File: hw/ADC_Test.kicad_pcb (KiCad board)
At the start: 2 copper layers, 50 x 32 mm, 63 parts, among them J1 SMA in (perfboard), J2 9V IN, J3 PMOD (ZedBoard), U1 OPA2365, U2 OPA2365, U3 THS4531, U4 ADS7057, U5 AMS1117-3.3, U6 LM393, U7 AMS1117-5.0

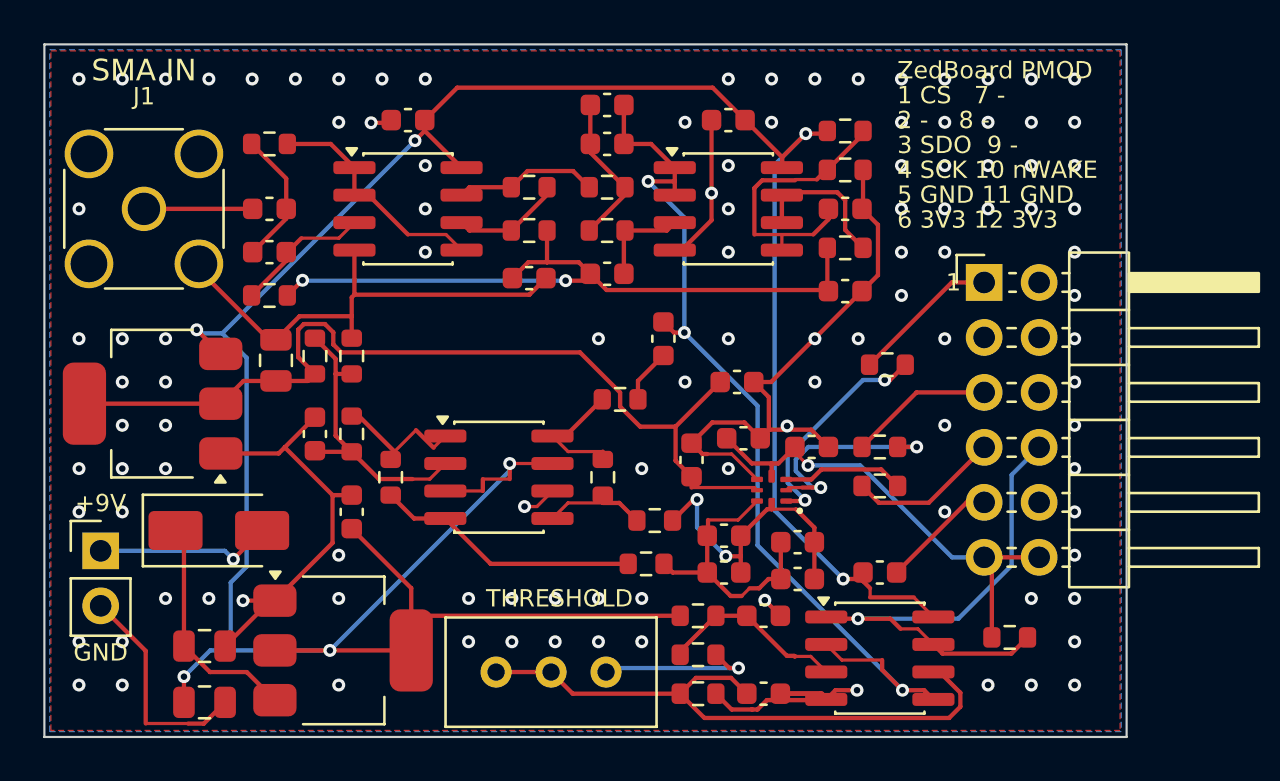
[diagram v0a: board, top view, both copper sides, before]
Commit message: Add MON output, nWAKE DNP cap, ceramic-stable AVDD LDO, M3 holes
- J4 SMA MON: LPF_OUT through 51R (Basic C23197)
- C31 0603 DNP on nWAKE near J3
- AVDD: XC6206P332 (Basic, ceramic-stable) replaces AMS1117-3.3
- 5 V AMS1117: 22 uF tantalum output per datasheet
- H1/H2 M3 holes, CH silkscreen field, PMOD legend on the back
- README: uses, regulator decision, MON/DNP

Co-Authored-By: Claude Opus 5.5 <noreply@anthropic.com>
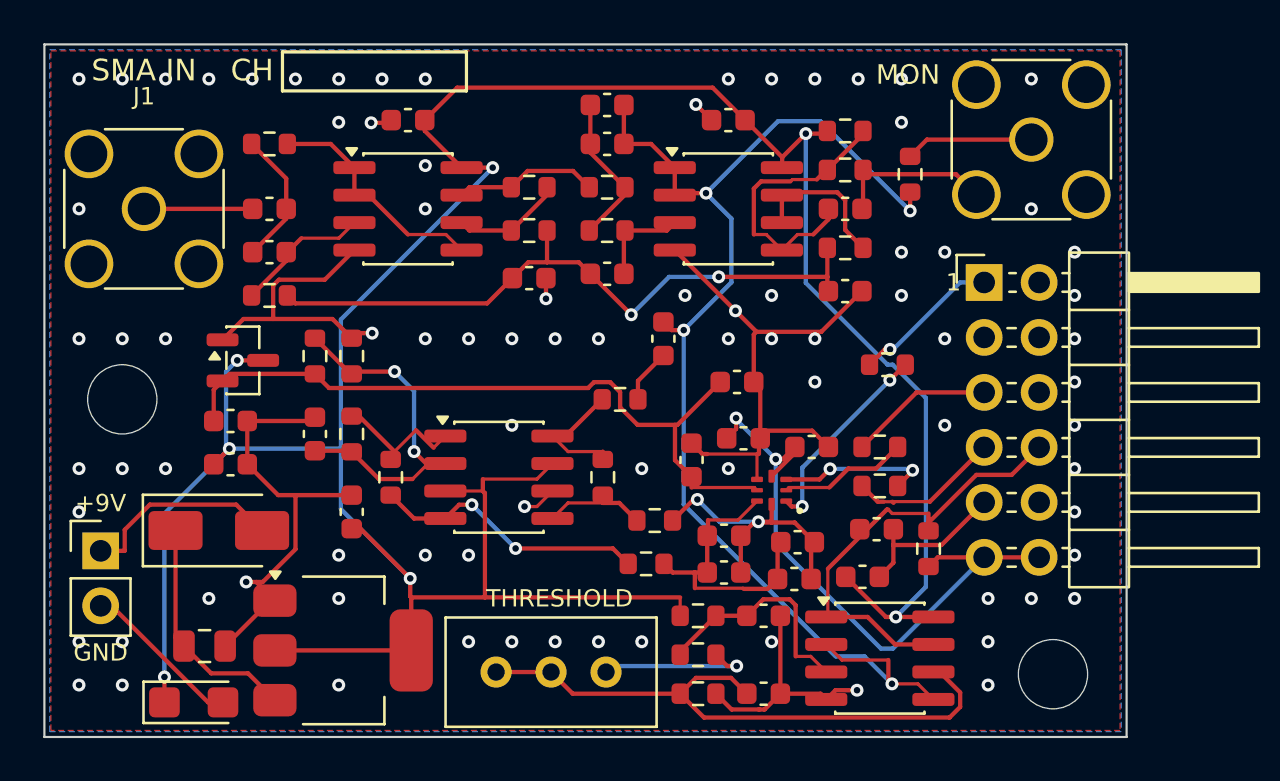
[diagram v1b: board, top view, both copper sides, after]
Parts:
- removed C24: 22uF 25V, Capacitor_SMD:C_0805_2012Metric
- added C29: 22uF 10V tantalum, Capacitor_Tantalum_SMD:CP_EIA-3216-18_Kemet-A, F.Cu at (106.9, 130.4)
- added C30: 1uF, Capacitor_SMD:C_0603_1608Metric, F.Cu at (108.6, 119.4)
- added C31: DNP, Capacitor_SMD:C_0603_1608Metric, F.Cu at (138.4, 122.4)
- added H1: M3, MountingHole:MountingHole_3.2mm_M3, F.Cu at (103.6, 116.4)
- added H2: M3, MountingHole:MountingHole_3.2mm_M3, F.Cu at (146.6, 129.1)
- added J4: SMA MON (hand-solder), Connector_Coaxial:SMA_Amphenol_132134_Vertical, F.Cu at (145.6, 104.4)
- added R25: 51R, Resistor_SMD:R_0603_1608Metric, F.Cu at (140.0, 106.0)
- C21: value 22uF 25V -> 1uF; footprint Capacitor_SMD:C_0805_2012Metric -> Capacitor_SMD:C_0603_1608Metric
- U5: value AMS1117-3.3 -> XC6206P332MR-G; footprint Package_TO_SOT_SMD:SOT-223-3_TabPin2 -> Package_TO_SOT_SMD:SOT-23
- moved R24 5.56 mm to (140.8, 123.3), turned to 90 degrees
- moved U5 4.62 mm to (109.2, 114.6), turned to 0 degrees
- moved C21 3.50 mm to (108.6, 117.4), turned to 0 degrees
- moved C28 0.82 mm to (137.8, 124.6)
- moved C17 0.15 mm to (134.7, 124.7)
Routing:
- net LPF_OUT: track 42.9 -> 57.3 mm, vias 3 -> 4
- net GND: track 107.0 -> 97.0 mm, vias 109 -> 84
- net AVDD: track 42.9 -> 33.9 mm
- net +3V3: track 21.6 -> 29.3 mm, vias 1 -> 2
- net MON: track 0.00 -> 5.92 mm
- net +5V: track 136.2 -> 141.3 mm
- net SDO_A: track 10.4 -> 5.98 mm, vias 2 -> 0
- net WAKE_N: track 24.4 -> 21.5 mm, vias 1 -> 0
- net VOCM: track 13.6 -> 16.2 mm, vias 0 -> 2
- net VMID5: track 33.3 -> 31.1 mm
- net VTH_H: track 8.66 -> 10.7 mm
- net SCLK_A: track 5.66 -> 7.07 mm, vias 0 -> 2
- net +9V_IN: track 8.17 -> 9.41 mm, vias 1 -> 0
- net CS_A: track 10.5 -> 9.37 mm
- net AINP: track 13.1 -> 13.7 mm
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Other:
- board text added: "CH"
- board text added: "MON"
- board text added: "ZedBoard PMOD (J3)"
- board text removed: "ZedBoard PMOD"

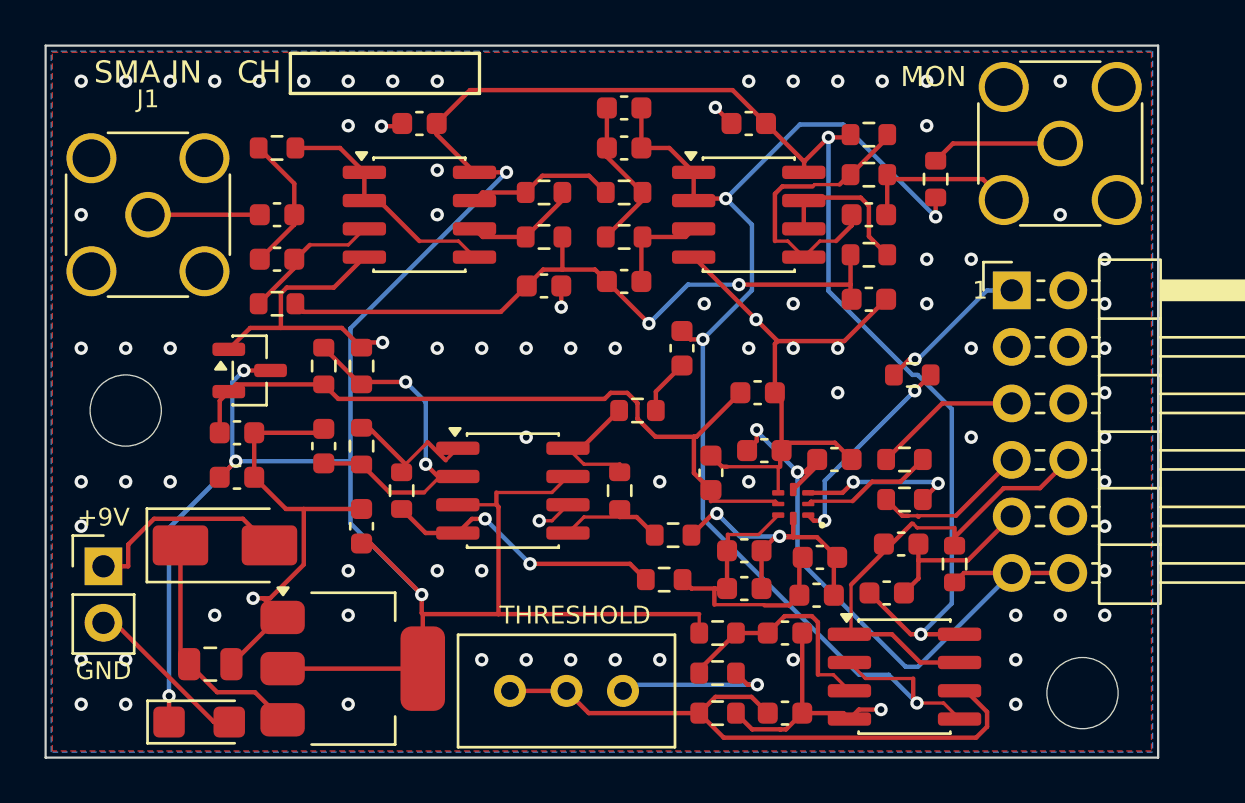
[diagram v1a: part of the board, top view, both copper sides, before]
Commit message: Put through-hole parts back in the JLC assembly, apply JLC rotation offsets
- BOM/CPL now include J1-J4 and RV1 (C496549, C492401, C60565, C34845)
- CPL rotations: SOIC +270, SOT-23 -90, SOT-223 +180, tantalum +180
- cost.py reads the BOM and compares JLC-soldered vs self-soldered THT
- finish.py: removes dangling GND stubs, solid GND connection for
  starved thermal pads, joint counts exported by fab.sh
- README: cost table for 2/3/5 boards, through-hole section

Co-Authored-By: Claude Sonnet 5.5 <noreply@anthropic.com>
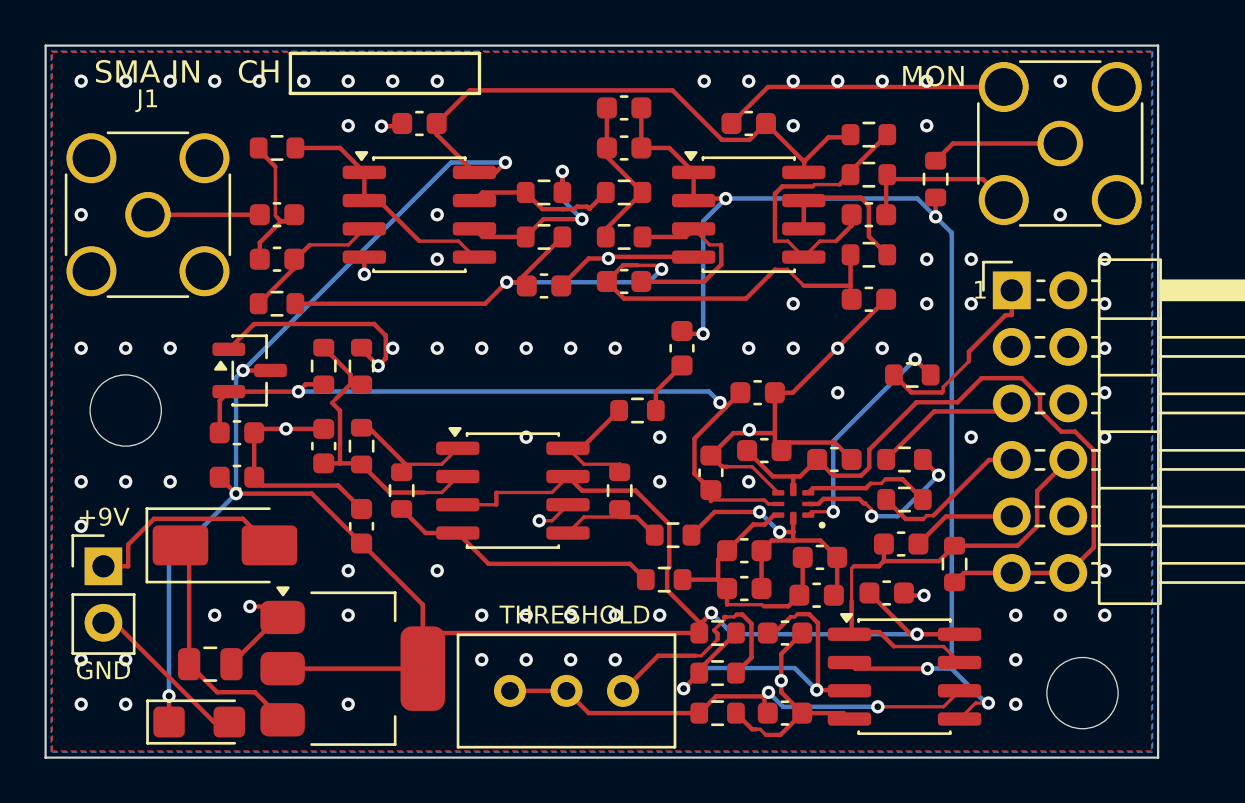
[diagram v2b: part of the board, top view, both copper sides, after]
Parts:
- J4: value SMA MON (hand-solder) -> SMA MON
- RV1: value 20k trim (hand-solder) -> 20k trim
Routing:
- net +5V: track 141.3 -> 125.8 mm, vias 7 -> 6
- net VTH_H: track 10.7 -> 17.5 mm, vias 0 -> 2
- net VMID5: track 31.1 -> 37.9 mm
- net VTH_L: track 28.5 -> 22.4 mm, vias 0 -> 2
- net LP_B: track 4.47 -> 8.79 mm
- net GN_FB: track 5.13 -> 8.77 mm, vias 0 -> 2
- net +3V3: track 29.3 -> 32.5 mm, vias 2 -> 0
- net PTOP: track 7.33 -> 10.4 mm, vias 1 -> 0
- net GND: track 97.0 -> 99.9 mm, vias 84 -> 90
- net VOCM: track 16.2 -> 13.6 mm, vias 2 -> 0
- net LPF_OUT: track 57.3 -> 54.7 mm, vias 4 -> 5
- net SDO_A: track 5.98 -> 8.22 mm, vias 0 -> 2
- net CS: track 6.87 -> 8.53 mm, vias 1 -> 0
- net SCLK_A: track 7.07 -> 5.79 mm, vias 2 -> 0
- net CS_A: track 9.37 -> 10.5 mm
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
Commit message: Silkscreen labels and logo, SMA 3D model, ngspice check
- front labels: SENSOR IN, SCOPE OUT, WAKE LEVEL, +9V/GND, CH box
- Auselia mark and name on the front, title on the back
- SMA footprint: 132134-11 (same pads, KiCad ships its 3D model)
- sim/adc_chain.py: DC, AC, noise and comparator window check
- README: silkscreen legend and simulation results

Co-Authored-By: Claude Sonnet 5.5 <noreply@anthropic.com>
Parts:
- J1, J4: footprint Connector_Coaxial:SMA_Amphenol_132134_Vertical -> Connector_Coaxial:SMA_Amphenol_132134-11_Vertical
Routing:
- net GND: track 99.9 -> 117.6 mm, vias 90 -> 82
- net +3V3: track 32.5 -> 22.1 mm, vias 0 -> 1
- net WAKE_N: track 21.9 -> 29.8 mm, vias 0 -> 1
- net VTH_H: track 17.5 -> 11.0 mm, vias 2 -> 0
- net AINP: track 12.6 -> 17.3 mm
- net LP_B: track 8.79 -> 4.47 mm
- net LPF_OUT: track 54.7 -> 58.7 mm
- net PTOP: track 10.4 -> 7.05 mm
- net AVDD: track 35.0 -> 37.5 mm
- net AINM: track 13.7 -> 12.1 mm, vias 2 -> 0
- net +5V: track 125.8 -> 124.2 mm
- net +9V_IN: track 9.41 -> 8.12 mm, vias 0 -> 1
- net VMID5: track 37.9 -> 37.2 mm
- net SCLK: track 7.11 -> 7.05 mm, vias 0 -> 1
- net VTH_L: track 22.4 -> 22.3 mm, vias 2 -> 0
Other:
- board text added: "AUSELIA"
- board text added: "SCOPE OUT"
- board text added: "SENSOR IN"
- board text added: "TEST v1"
- board text added: "WAKE LEVEL"
- board text removed: "MON"
- board text removed: "SMA IN"
- board text removed: "THRESHOLD"

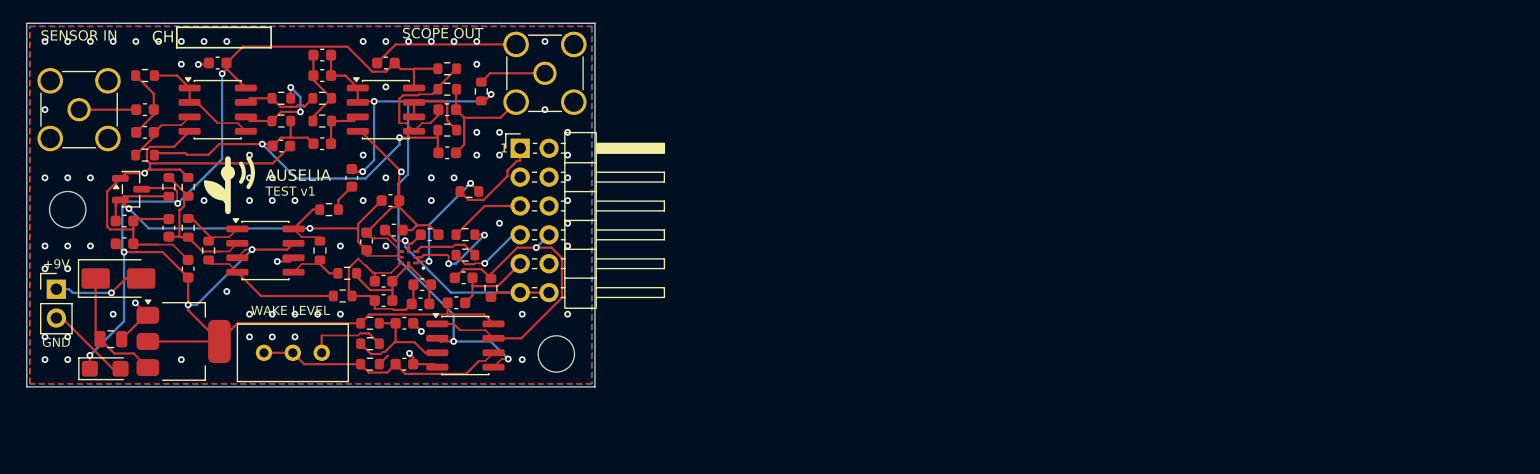
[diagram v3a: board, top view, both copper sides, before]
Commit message: Sensor head board with bias-T (HEAD IN), two separate boards, manual v0.2
- ADC_Head: perfboard charge amp (OPA365, 47 pF, 1M) on 10 x 22 mm, powered through the coax
- ADC_Test: 64 x 32 mm, new HEAD IN SMA with bias-T (L2, R26, C32, C33, R27), SENSOR IN kept
- build scripts take BOARD=head, two sets of fab files, cost model for two orders
- sim/head_bias_t.py (OPA365 model), sim/ths4531_stability_estimate.py
- manual v0.2: board figures regenerated, new section 9 (steps 55 to 60), top view page

Co-Authored-By: Claude Sonnet 5.5 <noreply@anthropic.com>
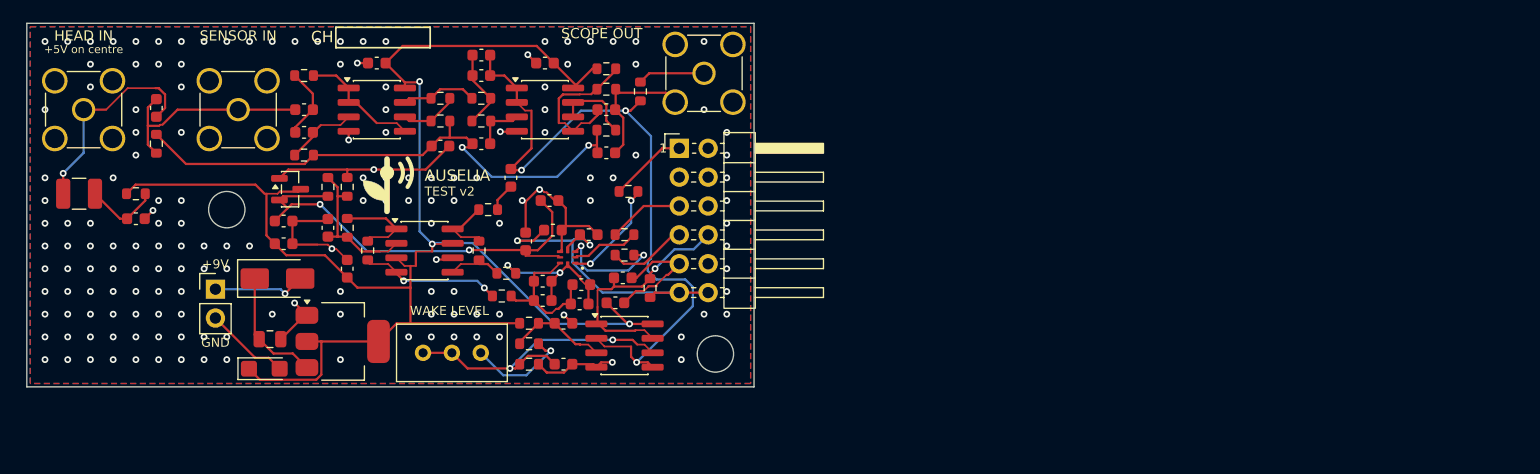
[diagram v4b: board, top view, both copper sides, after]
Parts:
- added C32: 10uF, Capacitor_SMD:C_0603_1608Metric, F.Cu at (109.6, 117.2)
- added C33: 100nF, Capacitor_SMD:C_0603_1608Metric, F.Cu at (111.4, 107.5)
- added J5: SMA HEAD IN, Connector_Coaxial:SMA_Amphenol_132134-11_Vertical, F.Cu at (105.0, 107.6)
- added L2: 470uH, Inductor_SMD:L_1210_3225Metric, F.Cu at (104.6, 115.0)
- added R26: 47R, Resistor_SMD:R_0603_1608Metric, F.Cu at (109.6, 115.0)
- added R27: 1M, Resistor_SMD:R_0603_1608Metric, F.Cu at (111.4, 110.6)
- moved C3 14.0 mm to (130.8, 103.5)
- moved R13 14.0 mm to (139.8, 120.0)
- moved R16 14.0 mm to (141.8, 124.0)
- moved U1 14.0 mm to (130.8, 107.6)
- moved C1 14.0 mm to (124.4, 107.6)
- moved C10 14.0 mm to (145.6, 103.5)
- moved C11 14.0 mm to (142.6, 113.6)
- moved C13 14.0 mm to (126.5, 118.0)
- moved C14 14.0 mm to (145.4, 122.7)
- moved C15 14.0 mm to (145.4, 124.4)
- moved C16 14.0 mm to (148.8, 123.0)
- moved C17 14.0 mm to (148.7, 124.7)
- moved C18 14.0 mm to (143.9, 119.2)
- moved C19 14.0 mm to (146.3, 118.2)
- moved C2 14.0 mm to (124.4, 109.6)
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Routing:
- net GND: track 117.6 -> 92.5 mm, vias 82 -> 161
- net HEAD_LINE: track 0.00 -> 18.6 mm, vias 0 -> 1
- net +5V: track 124.2 -> 141.7 mm, vias 6 -> 3
- net SIG_IN: track 5.03 -> 18.9 mm
- net VMID5: track 37.2 -> 48.7 mm
- net WAKE_N: track 29.8 -> 21.2 mm
- net +3V3: track 22.1 -> 30.2 mm, vias 1 -> 2
- net HEAD_PWR: track 0.00 -> 6.60 mm
- net VTH_L: track 22.3 -> 27.0 mm, vias 0 -> 2
- net AINP: track 17.3 -> 13.0 mm
- net SCLK_A: track 5.77 -> 9.50 mm, vias 0 -> 2
- net GN_FB: track 8.75 -> 5.13 mm, vias 2 -> 0
- net LPF_OUT: track 58.7 -> 62.2 mm, vias 5 -> 3
- net SDO_A: track 8.71 -> 5.98 mm, vias 2 -> 0
- net VTH_H: track 11.0 -> 8.66 mm
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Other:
- board size 50 x 32 mm -> 64 x 32 mm
- board text added: "+5V on centre"
- board text added: "ADS7057 test board v2"
- board text added: "HEAD IN"
- board text added: "TEST v2"
- board text removed: "ADS7057 test board v1"
- board text removed: "TEST v1"

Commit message: One SMA input: the bias-T sits on SENSOR IN (J1), HEAD IN removed; board back to 57 x 32 mm, re-placed and re-routed; manual and README updated
Co-Authored-By: Claude Sonnet 5.5 <noreply@anthropic.com>
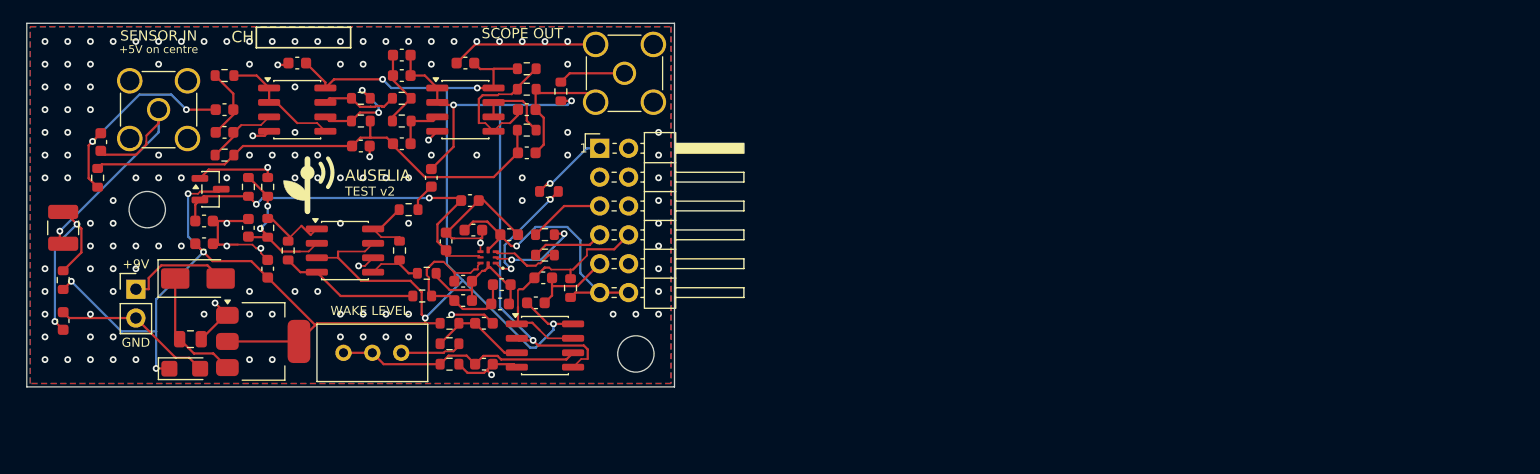
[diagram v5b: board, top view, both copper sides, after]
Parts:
- removed J5: SMA HEAD IN, Connector_Coaxial:SMA_Amphenol_132134-11_Vertical
- J1: value SMA in (perfboard) -> SMA SENSOR IN
- moved C32 11.0 mm to (103.2, 126.2), turned to 90 degrees
- moved R26 9.94 mm to (103.2, 122.6), turned to 90 degrees
- moved C3 7.00 mm to (123.8, 103.5)
- moved U1 7.00 mm to (123.8, 107.6)
- moved C1 7.00 mm to (117.4, 107.6)
- moved C10 7.00 mm to (138.6, 103.5)
- moved C11 7.00 mm to (135.6, 113.6)
- moved C13 7.00 mm to (119.5, 118.0)
- moved C14 7.00 mm to (138.4, 122.7)
- moved C15 7.00 mm to (138.4, 124.4)
- moved C16 7.00 mm to (141.8, 123.0)
- moved C17 7.00 mm to (141.7, 124.7)
- moved C18 7.00 mm to (136.9, 119.2)
- moved C19 7.00 mm to (139.3, 118.2)
- moved C2 7.00 mm to (117.4, 109.6)
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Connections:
- J1 pad 1: SIG_IN -> HEAD_LINE
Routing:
- net HEAD_PWR: track 6.60 -> 17.0 mm, vias 0 -> 2
- net GND: track 92.5 -> 99.8 mm, vias 161 -> 134
- net LPF_OUT: track 62.2 -> 56.3 mm
- net +3V3: track 30.2 -> 24.9 mm, vias 2 -> 1
- net VTH_L: track 27.0 -> 21.9 mm, vias 2 -> 0
- net HEAD_LINE: track 18.6 -> 23.6 mm
- net AVDD: track 39.8 -> 34.9 mm
- net VMID5: track 48.7 -> 44.0 mm, vias 2 -> 0
- net AINP: track 13.0 -> 16.9 mm
- net PTOP: track 9.22 -> 5.52 mm, vias 1 -> 0
- net GN_FB: track 5.13 -> 8.70 mm, vias 0 -> 2
- net SCLK_A: track 9.50 -> 6.05 mm, vias 2 -> 0
- net +5V: track 141.7 -> 145.1 mm, vias 3 -> 8
- net SDO_A: track 5.98 -> 8.11 mm, vias 0 -> 2
- net AINM: track 14.3 -> 12.2 mm, vias 2 -> 0
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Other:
- board size 64 x 32 mm -> 57 x 32 mm
- board text removed: "HEAD IN"
